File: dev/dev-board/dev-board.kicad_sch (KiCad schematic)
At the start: 35 parts, among them Q1 BSS138, Q2 BSS138, Q3 BSS138, Q4 BSS138, SW1 TS342A2P, SW2 TS342A2P, SW3 TS342A2P, SW4 TS342A2P, U1 ESP32-WROVER-IE(16MB), U2 ESP32-S3-WROOM-1(N16R8), U3 CP2105-F01-GMR, U4 TPS2065CDBV, U5 AP7361C-33E, U6 PESD5V0U2BT, U7 PESD5V0S1BA_C5261083

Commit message: making CAD
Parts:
- added C33, C34: 0.1uF, Capacitor_SMD:C_0603_1608Metric, symbol Device:C
- added C35, C36: 22uF, Capacitor_SMD:C_0603_1608Metric, symbol Device:C
- added D2: LED RED, LED_SMD:LED_0603_1608Metric, symbol Device:LED
- added R10, R11: 10K, Resistor_SMD:R_0603_1608Metric, symbol Device:R
- added R12: 100, Resistor_SMD:R_0603_1608Metric, symbol Device:R
- added R35: 1K, Resistor_SMD:R_0603_1608Metric, symbol Device:R
- C1: value C -> 0.1uF; footprint (none) -> Capacitor_SMD:C_0603_1608Metric
- C11, C2, C4, C5, C6: footprint (none) -> Capacitor_SMD:C_0603_1608Metric
- C12: value 0.1uF -> DNP; footprint (none) -> Capacitor_SMD:C_0603_1608Metric; now not fitted
- C3: value C -> 10uF; footprint (none) -> Capacitor_SMD:C_0603_1608Metric
- C7, C8: value 0.1u -> 0.1uF; footprint (none) -> Capacitor_SMD:C_0603_1608Metric
- R1, R2, R3, R4, R5, R6, R7, R8, R9: footprint (none) -> Resistor_SMD:R_0603_1608Metric
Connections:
- net S3-RX0 is gone; now on net RXD-ECI: U2.36 (RXD0)
- net S3-TX0 is gone; now on net TXD-ECI: U2.37 (TXD0)
- net WOVER-IO0 is gone; now on net WR-IO0: C12.2, SW2.2
- net WROVER-IO0 is gone; now on net WR-IO0: Q2.3 (D)
- net +3V3: now also C33.1, C34.1, C35.1, C36.1, R11.1, R35.1
- net GND: now also C1.2, C2.2, C3.2, C4.1, C5.1, C6.1, R1.1, U3.2 (GND), U4.2 (GND), U5.2 (GND), C33.2, C34.2, C35.2, C36.2, D2.1 (K)
- net RTS-SCI: no longer C7.1, Q1.3 (D), R8.2, SW4.2, U1.3 (EN)
- net RXD-SCI: now also U1.34 (RXD0)
- net SPI-CS0: now also U1.36 (IO22), R11.2
- net SPI-MISO: now also U1.30 (IO18)
- net SPI-MOSI: now also U1.33 (IO21)
- net SPI-SCLK: now also U1.31 (IO19)
- net TXD-SCI: now also U1.35 (TXD0)
- net VBUS: now also R10.1
- net WR-NTSC: now reaches U1.10 (IO25)
- net VSPI-DC: now reaches U1.11 (IO26)
- net WR-I2S-DOUT: now reaches U1.12 (IO27)
- net VSPI-MOSI: now reaches U1.13 (IO14)
- net VSPI-SCLK: now reaches U1.16 (IO13)
- net VSPI-TFT-RESET: now reaches U1.23 (IO15)
- net WR-IO0: now reaches U1.25 (IO0)
- net VSPI-CS: now reaches U1.26 (IO4)
- net VSPI-MISO: now reaches U1.37 (IO23)
- net WR-IO36: now reaches U1.4 (SENSOR_VP)
- net WR-IO39: now reaches U1.5 (SENSOR_VN)
- net WR-IO34: now reaches U1.6 (IO34)
- net WR-IO35: now reaches U1.7 (IO35)
- net WR-I2S-BLK: now reaches U1.8 (IO32)
- net WR-I2S-WS: now reaches U1.9 (IO33)
- net at U4.3 (~{FLT}): now also R10.2
- net S3-IO1 renamed S3-USB-PWSW
- net S3-IO14 renamed S3-I2C1-SDA
- net S3-IO15 renamed S3-SPI3-CS0
- net S3-IO16 renamed S3-SPI3-MOSI
- net S3-IO17 renamed S3-SPI3-SCLK
- net S3-IO18 renamed S3-SPI3-MISO
- net S3-IO19 renamed S3-USB-D-
- net S3-IO2 renamed S3-RMT
- net S3-IO20 renamed S3-USB-D+
- net S3-IO21 renamed S3-I2C1-SCL
- net S3-IO3: no longer names the net of U2.15 (IO3)
- net S3-IO38 renamed S3-SD-CD
- net S3-IO39 renamed S3-MTCK
- net S3-IO4 renamed S3-StatLED1
- net S3-IO40 renamed S3-MTDO
- net S3-IO41 renamed S3-MTDI
- net S3-IO42 renamed S3-MTMS
- net S3-IO47 renamed S3-I2C2-SDA
- net S3-IO48 renamed S3-I2C2-SCL
- net S3-IO5 renamed S3-ResetSub
- net S3-ResetSub: now also R12.1
- net S3-IO6 renamed S3-ButtonUp
- net S3-IO7 renamed S3-ButtonDown
- net S3-IO8 renamed S3-ButtonEnter
- net S3-IO9 renamed S3-ButtonCancel
- new net: D2.2 (A), R35.2
- new net WR-EN: C7.1, Q1.3 (D), R12.2, R8.2, SW4.2, U1.3 (EN)
- no-connect marks 32 -> 36
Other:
- sheet S3_peripheral ports: added ButtonCancel, ButtonDown, ButtonEnter, ButtonUp, I2C1-SCL, I2C1-SDA, I2C2-SCL, I2C2-SDA, MTCK, MTDI, MTDO, MTMS, RMT, SD-CD, SD-CS0, SD-MISO, SD-MOSI, SD-SCLK, StatLED1, USB-D+, USB-D-, USB-PWSW; removed S3-GPIO
- sheet wrover_peripheral ports: added I2S-BLK, I2S-DOUT, I2S-WS, IO34, IO35, IO36, IO39, NTSC, VSPI-CS, VSPI-DC, VSPI-MISO, VSPI-MOSI, VSPI-RESET, VSPI-SCLK; removed none
- note added: "ESP32電源用"
- note added: "USB側に120uF配置"
- note added: "オープンドレイン設定"
- moved on the sheet: C1, C2, C3, C7, C8, Q1, Q2, Q3, Q4, R2, R3, R4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

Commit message: finish cad. 1st step. add symbol,footprint files
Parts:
- D2: LCSC Part (none) -> C2286
- Q1, Q2, Q3, Q4: LCSC Part (none) -> C82045
- U4: LCSC Part (none) -> C353882
- U5: LCSC Part (none) -> C150719
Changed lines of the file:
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@@
+			)
+		)
+		(property "LCSC Part" "C150719"
+			(at 115.57 138.43 0)
+			(effects
+				(font
+					(size 1.27 1.27)
+				)
+				(hide yes)
 			)
 		)
@@
 		)
 		(property "Description" "50V Vds, 0.22A Id, N-Channel MOSFET, SOT-23"
+			(at 257.81 77.47 0)
+			(effects
+				(font
+					(size 1.27 1.27)
+				)
+				(hide yes)
+			)
+		)
+		(property "LCSC Part" "C82045"
 			(at 257.81 77.47 0)
 			(effects
@@
 			)
 		)
+		(property "LCSC Part" "C353882"
+			(at 77.47 140.97 0)
+			(effects
+				(font
+					(size 1.27 1.27)
+				)
+				(hide yes)
+			)
+		)
 		(pin "2"
 		)
@@
 			)
 		)
+		(property "LCSC Part" "C2286"
+			(at 138.43 147.32 90)
+			(effects
+				(font
+					(size 1.27 1.27)
+				)
+				(hide yes)
+			)
+		)
 		(pin "2"
 		)
@@
 			)
 		)
+		(property "LCSC Part" "C82045"
+			(at 201.93 93.98 0)
+			(effects
+				(font
+					(size 1.27 1.27)
+				)
+				(hide yes)
+			)
+		)
 		(pin "3"
 		)
@@
 			)
 		)
+		(property "LCSC Part" "C82045"
+			(at 201.93 77.47 0)
+			(effects
+				(font
+					(size 1.27 1.27)
+				)
+				(hide yes)
+			)
+		)
 		(pin "1"
 		)
@@
 			(at 257.81 93.98 0)
 			(effects
+				(font
+					(size 1.27 1.27)
+				)
+				(hide yes)
+			)
+		)
+		(property "LCSC Part" "C82045"
+			(at 257.81 93.98 0)
+			(effects

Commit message: complete BOM
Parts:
- removed USB1: TYPE-C 24P QCHT, easyeda2kicad:TYPE-C-SMD_TYPE-C-24P-QCHT, symbol easyeda2kicad:TYPE-C24PQCHT
- added USBC1: TYPE-C-31-M-12, easyeda2kicad:USB-C_SMD-TYPE-C-31-M-12_1_Small, symbol easyeda2kicad:TYPE-C-31-M-12
- C1, C11, C33, C34, C5, C7, C8: LCSC Part (none) -> C14663
- C2, C3: LCSC Part (none) -> C19702
- C35, C36: LCSC Part (none) -> C59461
- C4: LCSC Part (none) -> C15849
- C6: value 2uF -> 2.2uF; LCSC Part (none) -> C23630
- R1: LCSC Part (none) -> C23162
- R10, R11, R2, R3, R4, R5: LCSC Part (none) -> C25804
- R12: LCSC Part (none) -> C22775
- R35: LCSC Part (none) -> C21190
- R6, R7: LCSC Part (none) -> C23186
- R8, R9: value 10k -> 10K; LCSC Part (none) -> C25804
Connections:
- net CC1: now also USBC1.A5 (CC1)
- net CC2: now also USBC1.B5 (CC2)
- net D+: now also USBC1.A6 (DP1), USBC1.B6 (DP2)
- net D-: now also USBC1.A7 (DN1), USBC1.B7 (DN2)
- net GND: now also USBC1.1 (EH), USBC1.2 (EH), USBC1.3 (EH), USBC1.4 (EH), USBC1.A1B12 (GND), USBC1.B1A12 (GND)
- net VBUS: now also USBC1.A4B9 (VBUS), USBC1.B4A9 (VBUS)
- no-connect marks 36 -> 28

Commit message: fix LCSC num, improve cad
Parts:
- C35, C36: LCSC Part C59461 -> C84419
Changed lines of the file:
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@@
 			)
 		)
-		(property "LCSC Part" "C59461"
+		(property "LCSC Part" "C84419"
 			(at 167.64 142.24 0)
 			(effects
@@
 			)
 		)
-		(property "LCSC Part" "C59461"
+		(property "LCSC Part" "C84419"
 			(at 161.29 142.24 0)
 			(effects

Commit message: update schematics
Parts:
- removed U3: CP2105-F01-GMR, easyeda2kicad:QFN-24_L4.0-W4.0-P0.50-BL-EP2.6, symbol easyeda2kicad:CP2105-F01-GMR
- added C38: 0.1uF, Capacitor_SMD:C_0603_1608Metric, symbol Device:C
- added R37: 5.1K, Resistor_SMD:R_0603_1608Metric, symbol Device:R
- added R38: 10K, Resistor_SMD:R_0603_1608Metric, symbol Device:R
- added TP1, TP2, TP3, TP4: TestPoint, TestPoint:TestPoint_Pad_D1.0mm, symbol Connector:TestPoint
- added U14, U3: CH340C, easyeda2kicad:SOP-16_L10.0-W3.9-P1.27-LS6.0-BL, symbol easyeda2kicad:CH340C
- added U16: PESD5V0U2BT, easyeda2kicad:SOT-23-3_L2.9-W1.3-P1.90-LS2.4-BR, symbol easyeda2kicad:PESD5V0U2BT
- added USBC2: TYPE-C-31-M-12, easyeda2kicad:USB-C_SMD-TYPE-C-31-M-12_1_Small, symbol easyeda2kicad:TYPE-C-31-M-12
- C4: value 1uF -> 0.1uF; LCSC Part C15849 -> C14663
- C6: value 2.2uF -> 0.1uF; LCSC Part C23630 -> C14663
- R1: value 4.7K -> 5.1K; LCSC Part C23162 -> C23186
- R35: value 1K -> 2K; LCSC Part C21190 -> C22975
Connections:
- net S3-RMT is gone; now on net S3-ButtonCancel: U2.38 (IO2)
- net +3V3: now also C6.2, C38.2, R38.1, U14.16 (VCC), U3.16 (VCC)
- net GND: now also R1.2, C38.1, R37.2, U14.1 (GND), U16.3, U3.1 (GND), USBC2.1 (EH), USBC2.2 (EH), USBC2.3 (EH), USBC2.4 (EH), USBC2.A1B12 (GND), USBC2.B1A12 (GND); no longer R1.1
- net S3-ButtonCancel: no longer U2.17 (IO9)
- net VSYS: no longer C4.2
- net WR-IO12: now reaches U1.14 (IO12)
- net WR-IO5: now reaches U1.29 (IO5)
- net at C5.2: now also U14.4 (V3); no longer C6.2
- net CC1 renamed CC1-1
- net CC2 renamed CC2-1
- net D+ renamed D+1
- net D+1: now also U3.5 (D+)
- net D- renamed D-1
- net D-1: now also U3.6 (D-)
- net DTR-ECI renamed DTR1
- net DTR1: now also U3.13 (~{DTR})
- net DTR-SCI renamed DTR2
- net DTR2: now also U14.13 (~{DTR})
- net RTS-ECI renamed RTS1
- net RTS1: now also U3.14 (~{RTS})
- net RTS-SCI renamed RTS2
- net RTS2: now also U14.14 (~{RTS})
- net RXD-ECI renamed TX1
- net TX1: now also TP1.1, U3.2 (TXD)
- net RXD-SCI renamed TX2
- net TX2: now also TP2.1, U14.2 (TXD)
- net TXD-ECI renamed RX1
- net RX1: now also TP3.1, U3.3 (RXD)
- net TXD-SCI renamed RX2
- net RX2: now also TP4.1, U14.3 (RXD)
- net VSPI-CS renamed WR-IO4
- net VSPI-DC renamed WR-IO26
- net VSPI-MISO renamed SPI-SYNC
- net SPI-SYNC: now also U2.17 (IO9), R38.2
- net VSPI-MOSI renamed WR-IO14
- net VSPI-SCLK renamed WR-IO13
- net VSPI-TFT-RESET renamed WR-IO15
- new net: C4.2, U3.4 (V3)
- new net CC1-2: R1.1, USBC2.A5 (CC1)
- new net CC2-2: R37.1, USBC2.B5 (CC2)
- new net D+2: U14.5 (D+), U16.2, USBC2.A6 (DP1), USBC2.B6 (DP2)
- new net D-2: U14.6 (D-), U16.1, USBC2.A7 (DN1), USBC2.B7 (DN2)
- no-connect marks 28 -> 36
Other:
- sheet S3_peripheral ports: added none; removed RMT
- sheet wrover_peripheral ports: added IO12, IO13, IO14, IO15, IO26, IO4, IO5; removed VSPI-CS, VSPI-DC, VSPI-MISO, VSPI-MOSI, VSPI-RESET, VSPI-SCLK
- moved on the sheet: C1, C11, C12, C2, C3, C33, C34, C35, C36, C7, C8, D2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

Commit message: r2 candidate
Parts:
- RX1: renamed from TP3; now not fitted; now left out of the parts list
- RX2: renamed from TP4; now not fitted; now left out of the parts list
- TX1: renamed from TP1; now not fitted; now left out of the parts list
- TX2: renamed from TP2; now not fitted; now left out of the parts list
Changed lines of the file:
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@@
 		(unit 1)
 		(exclude_from_sim no)
-		(in_bom yes)
+		(in_bom no)
 		(on_board yes)
-		(dnp no)
+		(dnp yes)
 		(fields_autoplaced yes)
-		(property "Reference" "TP3"
+		(property "Reference" "RX1"
 			(at 189.23 103.6319 0)
 			(effects
@@
 			(project ""
 				(path "/211ed859-fe40-48f4-82b7-6e05ddc77423"
-					(reference "TP3")
+					(reference "RX1")
 					(unit 1)
 				)
@@
 		(unit 1)
 		(exclude_from_sim no)
-		(in_bom yes)
+		(in_bom no)
 		(on_board yes)
-		(dnp no)
+		(dnp yes)
 		(fields_autoplaced yes)
-		(property "Reference" "TP2"
+		(property "Reference" "TX2"
 			(at 209.55 92.2019 0)
 			(effects
@@
 			(project ""
 				(path "/211ed859-fe40-48f4-82b7-6e05ddc77423"
-					(reference "TP2")
+					(reference "TX2")
 					(unit 1)
 				)
@@
 		(unit 1)
 		(exclude_from_sim no)
-		(in_bom yes)
+		(in_bom no)
 		(on_board yes)
-		(dnp no)
+		(dnp yes)
 		(fields_autoplaced yes)
-		(property "Reference" "TP4"
+		(property "Reference" "RX2"
 			(at 209.55 103.6319 0)
 			(effects
@@
 			(project ""
 				(path "/211ed859-fe40-48f4-82b7-6e05ddc77423"
-					(reference "TP4")
+					(reference "RX2")
 					(unit 1)
 				)
@@
 		(unit 1)
 		(exclude_from_sim no)
-		(in_bom yes)
+		(in_bom no)
 		(on_board yes)
-		(dnp no)
+		(dnp yes)
 		(fields_autoplaced yes)
-		(property "Reference" "TP1"
+		(property "Reference" "TX1"
 			(at 189.23 92.2019 0)
 			(effects
@@
 			(project ""
 				(path "/211ed859-fe40-48f4-82b7-6e05ddc77423"
-					(reference "TP1")
+					(reference "TX1")
 					(unit 1)
 				)

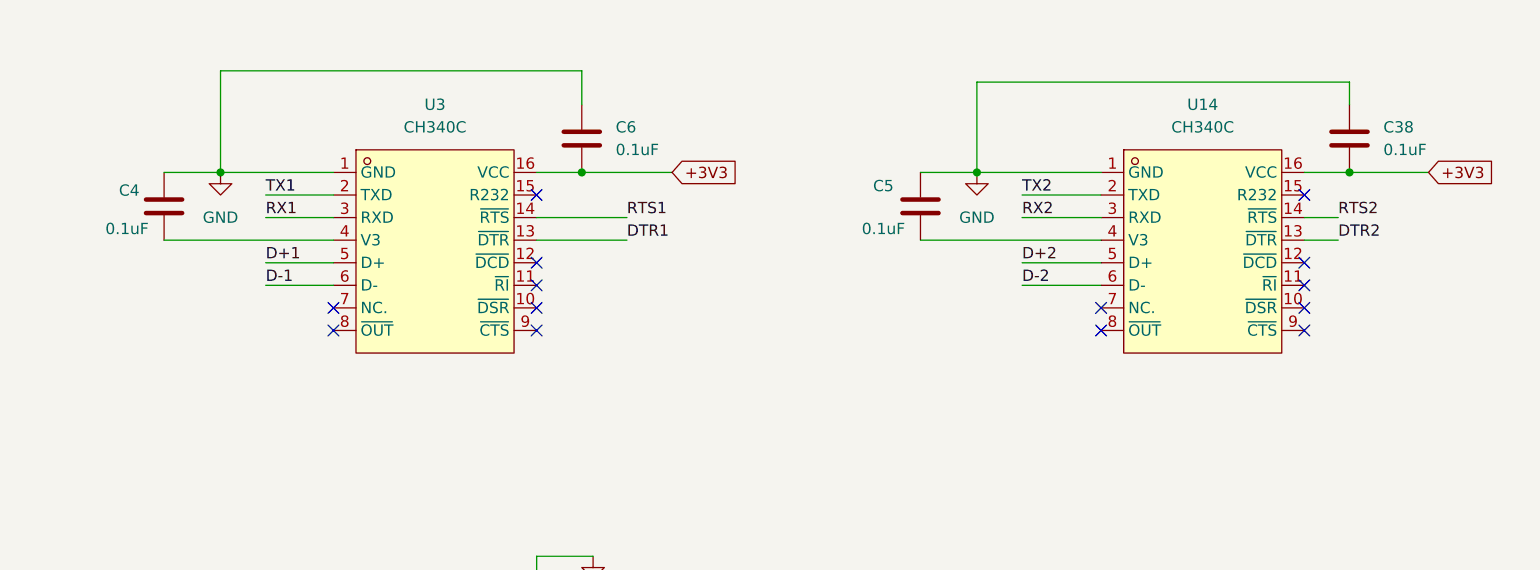
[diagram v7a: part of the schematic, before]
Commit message: r2 candidate (fix CH340 V3-VCC)
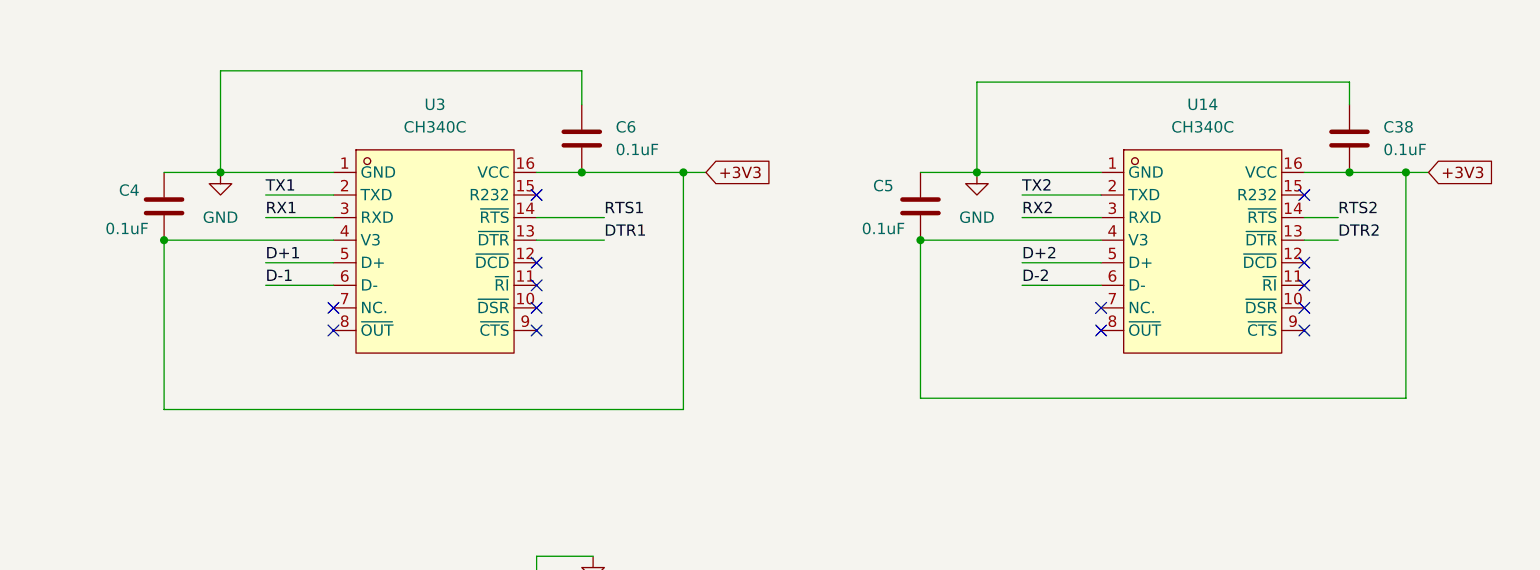
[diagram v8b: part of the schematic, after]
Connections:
- net +3V3: now also C4.2, C5.2, U14.4 (V3), U3.4 (V3)
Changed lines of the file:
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@@
 	)
 	(junction
+		(at 283.21 38.1)
+		(diameter 0)
+		(color 0 0 0 0)
+	)
+	(junction
 		(at 250.19 152.4)
 		(diameter 0)
@@
 	)
 	(junction
+		(at 364.49 38.1)
+		(diameter 0)
+		(color 0 0 0 0)
+	)
+	(junction
 		(at 231.14 38.1)
 		(diameter 0)
@@
 	)
 	(junction
+		(at 224.79 45.72)
+		(diameter 0)
+		(color 0 0 0 0)
+	)
+	(junction
 		(at 133.35 195.58)
 		(diameter 0)
@@
 	)
 	(junction
+		(at 309.88 45.72)
+		(diameter 0)
+		(color 0 0 0 0)
+	)
+	(junction
 		(at 99.06 133.35)
 		(diameter 0)
@@
 	(wire
 		(pts
+			(xy 283.21 38.1) (xy 285.75 38.1)
+		)
+		(stroke
+			(width 0)
+			(type default)
+		)
+	)
+	(wire
+		(pts
 			(xy 347.98 173.99) (xy 347.98 175.26)
 		)
@@
 	(wire
 		(pts
+			(xy 224.79 64.77) (xy 224.79 45.72)
+		)
+		(stroke
+			(width 0)
+			(type default)
+		)
+	)
+	(wire
+		(pts
+			(xy 364.49 38.1) (xy 367.03 38.1)
+		)
+		(stroke
+			(width 0)
+			(type default)
+		)
+	)
+	(wire
+		(pts
 			(xy 110.49 58.42) (xy 123.19 58.42)
 		)
@@
 	(wire
 		(pts
+			(xy 283.21 64.77) (xy 224.79 64.77)
+		)
+		(stroke
+			(width 0)
+			(type default)
+		)
+	)
+	(wire
+		(pts
 			(xy 83.82 133.35) (xy 87.63 133.35)
 		)
@@
 	(wire
 		(pts
-			(xy 266.7 45.72) (xy 276.86 45.72)
+			(xy 266.7 45.72) (xy 274.32 45.72)
 		)
 		(stroke
@@
 	(wire
 		(pts
-			(xy 358.14 38.1) (xy 367.03 38.1)
+			(xy 358.14 38.1) (xy 364.49 38.1)
 		)
 		(stroke
@@
 	(wire
 		(pts
+			(xy 364.49 63.5) (xy 309.88 63.5)
+		)
+		(stroke
+			(width 0)
+			(type default)
+		)
+	)
+	(wire
+		(pts
 			(xy 69.85 30.48) (xy 72.39 30.48)
 		)
@@
 	(wire
 		(pts
+			(xy 283.21 38.1) (xy 283.21 64.77)
+		)
+		(stroke
+			(width 0)
+			(type default)
+		)
+	)
+	(wire
+		(pts
 			(xy 316.23 233.68) (xy 331.47 233.68)
 		)
@@
 	(wire
 		(pts
+			(xy 309.88 63.5) (xy 309.88 45.72)
+		)
+		(stroke
+			(width 0)
+			(type default)
+		)
+	)
+	(wire
+		(pts
 			(xy 265.43 222.25) (xy 267.97 222.25)
 		)
@@
 	(wire
 		(pts
-			(xy 271.78 38.1) (xy 281.94 38.1)
+			(xy 271.78 38.1) (xy 283.21 38.1)
 		)
 		(stroke
@@
 	(wire
 		(pts
-			(xy 266.7 43.18) (xy 276.86 43.18)
+			(xy 266.7 43.18) (xy 274.32 43.18)
 		)
 		(stroke
@@
 	(wire
 		(pts
+			(xy 364.49 38.1) (xy 364.49 63.5)
+		)
+		(stroke
+			(width 0)
+			(type default)
+		)
+	)
+	(wire
+		(pts
 			(xy 22.86 151.13) (xy 26.67 151.13)
 		)
@@
 	)
 	(label "RTS1"
-		(at 276.86 43.18 0)
+		(at 274.32 43.18 0)
 		(effects
 			(font
@@
 	)
 	(label "DTR1"
-		(at 276.86 45.72 0)
+		(at 274.32 45.72 0)
 		(effects
 			(font
@@
 	(global_label "+3V3"
 		(shape input)
-		(at 281.94 38.1 0)
+		(at 285.75 38.1 0)
 		(fields_autoplaced yes)
 		(effects
@@
 		)
 		(property "Intersheetrefs" "${INTERSHEET_REFS}"
-			(at 290.0052 38.1 0)
+			(at 293.8152 38.1 0)
 			(effects
 				(font
